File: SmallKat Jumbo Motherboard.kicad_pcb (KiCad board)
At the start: 4 copper layers, 80 x 80 mm, 49 parts, among them IC1 TPS562201DDCR, IC2 TPS562201DDCR, J1 Conn_01x06_Male, J10 Conn_01x06_Male, J11 Conn_01x06_Male, J12 Conn_01x04_Male, J13 Conn_01x02_Male, J14 Conn_01x04_Male, J15 Conn_01x04_Male, J16 Conn_01x06_Male, J2 Conn_01x06_Male, J3 Conn_01x06_Male, J4 Conn_01x06_Male, J5 Conn_01x06_Male, J6 Conn_01x06_Male, J7 Conn_01x06_Male, J8 Conn_01x06_Male, J9 Conn_01x06_Male, U1 STM32H753IITx, Y1 32.768khz, Y2 32MHZ

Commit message: Added mounting holes
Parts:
- added REF**: MountingHole_3.2mm_M3, MountingHole:MountingHole_3.2mm_M3, F.Cu at (76.5, 3.50)
- added REF**: MountingHole_3.2mm_M3, MountingHole:MountingHole_3.2mm_M3, F.Cu at (3.50, 3.50)
- added REF**: MountingHole_3.2mm_M3, MountingHole:MountingHole_3.2mm_M3, F.Cu at (76.5, 76.5)
- added REF**: MountingHole_3.2mm_M3, MountingHole:MountingHole_3.2mm_M3, F.Cu at (3.50, 76.5)
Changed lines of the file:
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@@
     (tracks 1078)
     (zones 0)
-    (modules 49)
+    (modules 53)
     (nets 56)
   )
@@
     (add_net USBDP)
   )
+  (module MountingHole:MountingHole_3.2mm_M3 (layer F.Cu)
+    (at 76.5 3.5)
+    (descr "Mounting Hole 3.2mm, no annular, M3")
+    (tags "mounting hole 3.2mm no annular m3")
+    (attr virtual)
+    (fp_text reference REF** (at 0 -4.2) (layer F.SilkS)
+      (effects (font (size 1 1) (thickness 0.15)))
+    )
+    (fp_text value MountingHole_3.2mm_M3 (at 0 4.2) (layer F.Fab)
+      (effects (font (size 1 1) (thickness 0.15)))
+    )
+    (fp_circle (center 0 0) (end 3.45 0) (layer F.CrtYd) (width 0.05))
+    (fp_circle (center 0 0) (end 3.2 0) (layer Cmts.User) (width 0.15))
+    (fp_text user %R (at 0.3 0) (layer F.Fab)
+      (effects (font (size 1 1) (thickness 0.15)))
+    )
+    (pad 1 np_thru_hole circle (at 0 0) (size 3.2 3.2) (drill 3.2) (layers *.Cu *.Mask))
+  )
   (module Crystal:Crystal_SMD_2012-2Pin_2.0x1.2mm (layer F.Cu)
     (at 24.79 33.81 270)
@@
     )
   )
+  (module MountingHole:MountingHole_3.2mm_M3 (layer F.Cu)
+    (at 3.5 3.5)
+    (descr "Mounting Hole 3.2mm, no annular, M3")
+    (tags "mounting hole 3.2mm no annular m3")
+    (attr virtual)
+    (fp_text reference REF** (at 0 -4.2) (layer F.SilkS)
+      (effects (font (size 1 1) (thickness 0.15)))
+    )
+    (fp_text value MountingHole_3.2mm_M3 (at 0 4.2) (layer F.Fab)
+      (effects (font (size 1 1) (thickness 0.15)))
+    )
+    (fp_text user %R (at 0.3 0) (layer F.Fab)
+      (effects (font (size 1 1) (thickness 0.15)))
+    )
+    (fp_circle (center 0 0) (end 3.2 0) (layer Cmts.User) (width 0.15))
+    (fp_circle (center 0 0) (end 3.45 0) (layer F.CrtYd) (width 0.05))
+    (pad 1 np_thru_hole circle (at 0 0) (size 3.2 3.2) (drill 3.2) (layers *.Cu *.Mask))
+  )
+  (module MountingHole:MountingHole_3.2mm_M3 (layer F.Cu)
+    (at 76.5 76.5)
+    (descr "Mounting Hole 3.2mm, no annular, M3")
+    (tags "mounting hole 3.2mm no annular m3")
+    (attr virtual)
+    (fp_text reference REF** (at 0 -4.2) (layer F.SilkS)
+      (effects (font (size 1 1) (thickness 0.15)))
+    )
+    (fp_text value MountingHole_3.2mm_M3 (at 0 4.2) (layer F.Fab)
+      (effects (font (size 1 1) (thickness 0.15)))
+    )
+    (fp_circle (center 0 0) (end 3.45 0) (layer F.CrtYd) (width 0.05))
+    (fp_circle (center 0 0) (end 3.2 0) (layer Cmts.User) (width 0.15))
+    (fp_text user %R (at 0.3 0) (layer F.Fab)
+      (effects (font (size 1 1) (thickness 0.15)))
+    )
+    (pad 1 np_thru_hole circle (at 0 0) (size 3.2 3.2) (drill 3.2) (layers *.Cu *.Mask))
+  )
+  (module MountingHole:MountingHole_3.2mm_M3 (layer F.Cu)
+    (at 3.5 76.5)
+    (descr "Mounting Hole 3.2mm, no annular, M3")
+    (tags "mounting hole 3.2mm no annular m3")
+    (attr virtual)
+    (fp_text reference REF** (at 0 -4.2) (layer F.SilkS)
+      (effects (font (size 1 1) (thickness 0.15)))
+    )
+    (fp_text value MountingHole_3.2mm_M3 (at 0 4.2) (layer F.Fab)
+      (effects (font (size 1 1) (thickness 0.15)))
+    )
+    (fp_circle (center 0 0) (end 3.45 0) (layer F.CrtYd) (width 0.05))
+    (fp_circle (center 0 0) (end 3.2 0) (layer Cmts.User) (width 0.15))
+    (fp_text user %R (at 0.3 0) (layer F.Fab)
+      (effects (font (size 1 1) (thickness 0.15)))
+    )
+    (pad 1 np_thru_hole circle (at 0 0) (size 3.2 3.2) (drill 3.2) (layers *.Cu *.Mask))
+  )
   (gr_line (start 80 80) (end 80 0) (layer Edge.Cuts) (width 0.2))

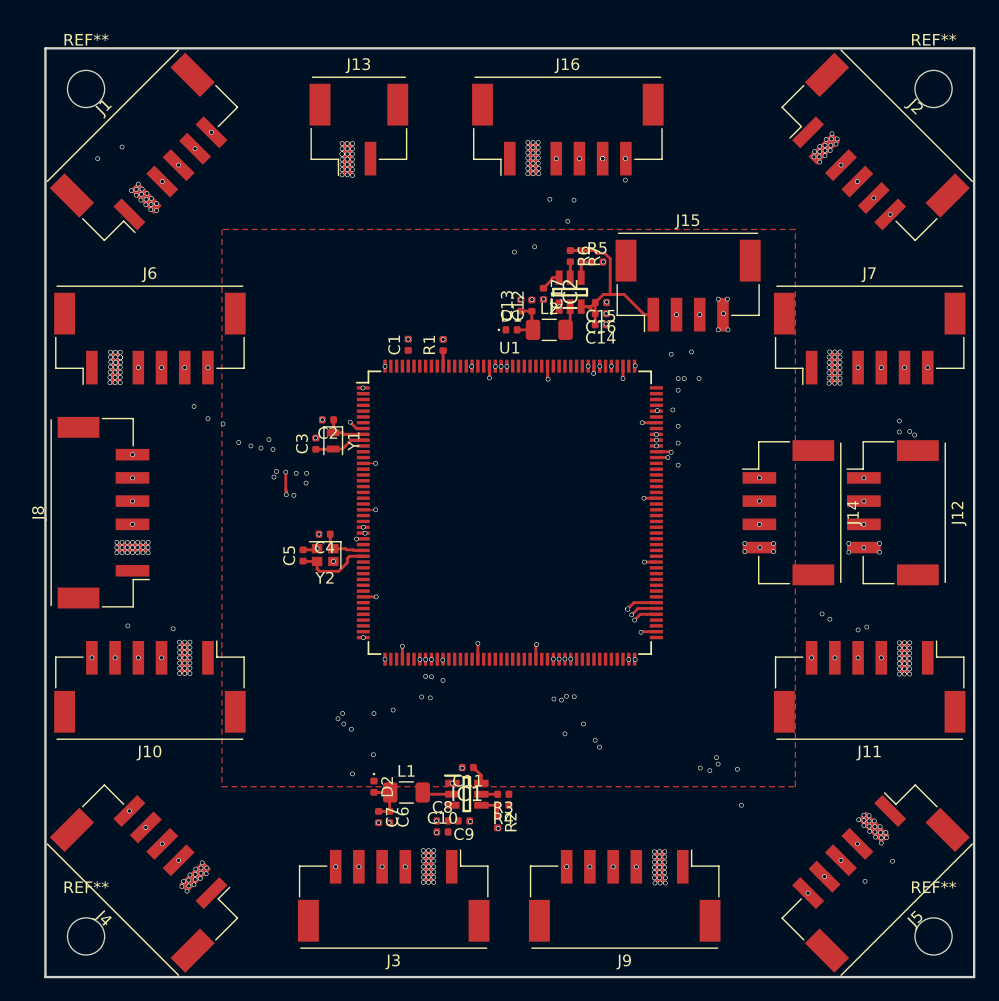
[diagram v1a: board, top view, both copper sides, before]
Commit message: fixed pinout
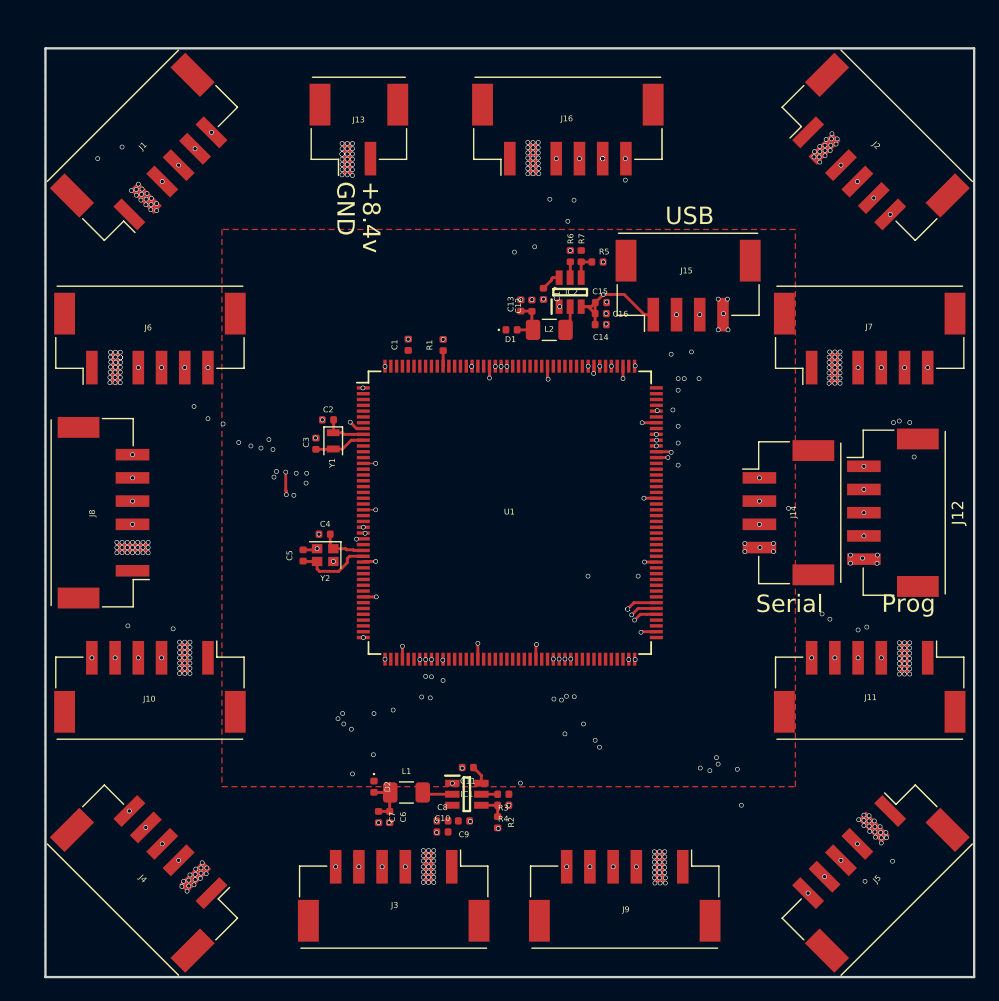
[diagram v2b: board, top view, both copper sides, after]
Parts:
- removed REF** (x4): MountingHole_3.2mm_M3, MountingHole:MountingHole_3.2mm_M3
- J12: value Conn_01x04_Male -> Conn_01x05_Male; footprint Connector_Molex:Molex_CLIK-Mate_502443-0470_1x04-1MP_P2.00mm_Vertical -> Connector_Molex:Molex_CLIK-Mate_502443-0570_1x05-1MP_P2.00mm_Vertical
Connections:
- J12 pad 1: SWCLK -> NRST
- J12 pad 2: SWDIO -> SWCLK
- J12 pad 3: +3V3 -> SWDIO
- J12 pad 4: GND -> +3V3
- R4 pad 1: +BATT -> +3V3
- R7 pad 1: +5V -> +3V3
- U1 pad 31: (no net) -> NRST
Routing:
- net NRST: track 0.00 -> 47.9 mm, vias 0 -> 5
- net +3V3: track 9.00 -> 11.7 mm, vias 2 -> 4
- net +5V: track 17.5 -> 15.7 mm, vias 0 -> 2
- net SCK5: track 123.7 -> 122.8 mm
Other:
- board text added: "+8.4v"
- board text added: "GND"
- board text added: "Keion Bisland Xavier Little Alex Tacescu"
- board text added: "Prog"
- board text added: "Serial"
- board text added: "SmallKat MQP Motherboard Rev. 1"
- board text added: "USB"

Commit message: Rev 2
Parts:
- removed C10, C11: 0.1UF, Capacitor_SMD:C_0402_1005Metric
- removed C15, C8, C9: 10UF, Capacitor_SMD:C_0402_1005Metric
- removed C6, C7: 22UF, Capacitor_SMD:C_0402_1005Metric
- removed IC1: TPS562201DDCR, TPS562201DDCR:SOT95P280X110-6N
- removed J11: Conn_01x06_Male, Connector_Molex:Molex_CLIK-Mate_502443-0670_1x06-1MP_P2.00mm_Vertical
- removed J12: Conn_01x05_Male, Connector_Molex:Molex_CLIK-Mate_502443-0570_1x05-1MP_P2.00mm_Vertical
- removed J13: Conn_01x02_Male, Connector_Molex:Molex_CLIK-Mate_502443-0270_1x02-1MP_P2.00mm_Vertical
- removed L1: 4.7UH, Inductor_SMD:L_1206_3216Metric
- added C18: 0.1uF, Capacitor_SMD:C_0402_1005Metric, F.Cu at (34.1, 43.3)
- added C19: 0.1uF, Capacitor_SMD:C_0402_1005Metric, F.Cu at (26.5, 29.8)
- added C20: 0.1uF, Capacitor_SMD:C_0402_1005Metric, F.Cu at (48.6, 35.4)
- added C21: 0.1uF, Capacitor_SMD:C_0402_1005Metric, F.Cu at (40.1, 21.3)
- added C22: 0.1uF, Capacitor_SMD:C_0402_1005Metric, F.Cu at (26.7, 35.9)
- added D3: LED, LED_SMD:LED_0603_1608Metric, F.Cu at (42.1, 16.9)
- added FB1: Ferrite_Bead, Inductor_SMD:L_0805_2012Metric, B.Cu at (24.2, 32.4)
- added H1: MountingHole, MountingHole:MountingHole_3.2mm_M3, F.Cu at (72.3, 61.0)
- added H2: MountingHole, MountingHole:MountingHole_3.2mm_M3, F.Cu at (71.1, 3.35)
- added H3: MountingHole, MountingHole:MountingHole_3.2mm_M3, F.Cu at (5.35, 13.3)
- added R10: 10k, Resistor_SMD:R_0402_1005Metric, F.Cu at (28.5, 27.0)
- added R11: 33R, Resistor_SMD:R_0402_1005Metric, F.Cu at (61.8, 54.0)
- added R12: 33R, Resistor_SMD:R_0402_1005Metric, F.Cu at (63.8, 54.1)
- added R8: 33R, Resistor_SMD:R_0402_1005Metric, F.Cu at (60.9, 10.2)
- added R9: 33R, Resistor_SMD:R_0402_1005Metric, F.Cu at (58.9, 10.2)
- C1: value 1UF -> 0.1uF
- C12, C13, C14, C16: footprint Capacitor_SMD:C_0402_1005Metric -> Capacitor_SMD:C_0805_2012Metric
- D1, D2: value 641-1675-1-ND -> LED; footprint Diode_SMD:D_0402_1005Metric -> LED_SMD:LED_0603_1608Metric
- J10, J9: value Conn_01x06_Male -> Conn_01x04_Male; footprint Connector_Molex:Molex_CLIK-Mate_502443-0670_1x06-1MP_P2.00mm_Vertical -> Connector_Molex:Molex_CLIK-Mate_502443-0470_1x04-1MP_P2.00mm_Vertical
- J8: value Conn_01x06_Male -> PRT-10474; footprint Connector_Molex:Molex_CLIK-Mate_502443-0670_1x06-1MP_P2.00mm_Vertical -> PRT-10474:SHDR2W320P716_1X2_1574X813X1588P
- L2: footprint Inductor_SMD:L_1206_3216Metric -> Inductor_SMD:L_0805_2012Metric_Pad1.15x1.40mm_HandSolder
- R1, R5: value 10K -> 10k
- R2, R3: value 10K -> 330R
- R4: value 33.2K -> 330R
- R7: value 33.2K -> 33.2k
- U1: value STM32H753IITx -> STM32H743VITx; footprint Package_QFP:LQFP-176_24x24mm_P0.5mm -> Package_QFP:LQFP-100_14x14mm_P0.5mm
- moved J5 71.0 mm to (5.00, 44.7), turned to 90 degrees
- moved J3 68.3 mm to (26.4, 4.80), turned to 0 degrees
- moved J1 62.8 mm to (46.2, 59.6), turned to 180 degrees
- moved J2 62.5 mm to (8.60, 4.80), turned to 0 degrees
- moved J10 54.0 mm to (62.8, 59.6)
- moved J9 49.5 mm to (70.1, 27.8), turned to 270 degrees
- moved D2 49.2 mm to (43.8, 16.9)
- moved R2 47.5 mm to (45.1, 19.5), turned to 90 degrees
- moved R4 45.8 mm to (42.1, 19.5), turned to 90 degrees
- moved R3 44.9 mm to (43.8, 19.6), turned to 90 degrees
- moved J6 39.2 mm to (27.4, 59.6), turned to 180 degrees
- moved J14 27.8 mm to (70.1, 12.9)
- moved C1 20.5 mm to (40.3, 44.0), turned to 225 degrees
- moved J7 19.9 mm to (70.2, 44.9), turned to 270 degrees
- moved J15 16.3 mm to (59.9, 4.80)
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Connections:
- C1 pad 2: GND -> MCU_GND
- C12 pad 1: Net-(C12-Pad1) -> +3V3
- C13 pad 1: Net-(C12-Pad1) -> +3V3
- C17 pad 2: GND -> Net-(C17-Pad2)
- C2 pad 2: GND -> MCU_GND
- C3 pad 2: GND -> MCU_GND
- C4 pad 2: GND -> MCU_GND
- C5 pad 2: GND -> MCU_GND
- D1 pad 1: +3V3 -> GND
- D1 pad 2: Net-(C12-Pad1) -> Net-(D1-Pad2)
- D2 pad 1: +3V3 -> GND
- D2 pad 2: Net-(C6-Pad1) -> Net-(D2-Pad2)
- IC2 pad 2: Net-(IC2-Pad2) -> Net-(C17-Pad2)
- J1 pad 3: SCK1 -> MISO1
- J1 pad 4: MISO1 -> MOSI1
- J1 pad 5: MOSI1 -> SCK1
- J1 pad 6: CS1_1 -> CS1
- J10 pad 1: +BATT -> +5V
- J10 pad 2: GND -> Net-(J10-Pad2)
- J10 pad 3: SCK5 -> Net-(J10-Pad3)
- J10 pad 4: MISO5 -> GND
- J15 pad 2: USBDM -> Net-(J15-Pad2)
- J15 pad 3: USBDP -> Net-(J15-Pad3)
- J16 pad 6: CS6 -> CS6_HEAD
- J2 pad 3: SCK1 -> MISO3
- J2 pad 4: MISO1 -> MOSI3
- J2 pad 5: MOSI1 -> SCK3
- J2 pad 6: CS1_2 -> CS3
- J3 pad 3: SCK2 -> SCK6
- J3 pad 4: MISO2 -> MISO6
- J3 pad 5: MOSI2 -> MOSI6
- J3 pad 6: CS2 -> CS6_TAIL
- J4 pad 3: SCK1 -> MISO2
- J4 pad 4: MISO1 -> MOSI2
- J4 pad 5: MOSI1 -> SCK2
- J4 pad 6: CS1_3 -> CS2
- J5 pad 3: SCK1 -> MISO4
- J5 pad 4: MISO1 -> MOSI4
- J5 pad 5: MOSI1 -> SCK4
- J5 pad 6: CS1_4 -> CS4
- J6 pad 3: SCK5 -> MISO1
- J6 pad 4: MISO5 -> MOSI1
- J6 pad 5: MOSI5 -> SCK1
- J6 pad 6: CS5_1 -> IMU1_CS
- J7 pad 3: SCK5 -> MISO2
- J7 pad 4: MISO5 -> MOSI2
- J7 pad 5: MOSI5 -> SCK2
- J7 pad 6: CS5_2 -> IMU2_CS
- J8 pad 1: +BATT -> GND
- J8 pad 2: GND -> +BATT
- J9 pad 1: +BATT -> SWCLK
- J9 pad 2: GND -> SWDIO
- J9 pad 3: SCK4 -> +3V3
- J9 pad 4: MISO4 -> GND
- L2 pad 1: Net-(C12-Pad1) -> +3V3
- L2 pad 2: Net-(IC2-Pad2) -> Net-(C17-Pad2)
- R2 pad 1: Net-(IC1-Pad4) -> LED1
- R2 pad 2: GND -> Net-(D1-Pad2)
- R3 pad 1: +BATT -> LED2
- R3 pad 2: Net-(IC1-Pad5) -> Net-(D2-Pad2)
- R4 pad 1: +3V3 -> LED3
- R4 pad 2: Net-(IC1-Pad4) -> Net-(D3-Pad2)
- U1 pad 1: CS5_1 -> SCK4
- U1 pad 10: OSCOUT_32 -> MCU_GND
- U1 pad 100: (no net) -> +3V3
- U1 pad 11: (no net) -> +3V3
- U1 pad 12: (no net) -> OSCIN
- U1 pad 13: (no net) -> OSCOUT
- U1 pad 14: GND -> Net-(U1-Pad14)
- U1 pad 15: +3V3 -> Net-(U1-Pad15)
- U1 pad 16: (no net) -> MOSI2
- U1 pad 17: (no net) -> MISO2
- U1 pad 18: (no net) -> CS2
- U1 pad 19: (no net) -> MCU_GND
- U1 pad 2: (no net) -> Net-(U1-Pad2)
- U1 pad 20: (no net) -> Net-(U1-Pad20)
- U1 pad 21: (no net) -> +3V3
- U1 pad 22: GND -> Net-(U1-Pad22)
- U1 pad 23: +3V3 -> IMU1_CS
- U1 pad 24: (no net) -> Net-(U1-Pad24)
- U1 pad 25: SCK5 -> Net-(U1-Pad25)
- U1 pad 26: MISO5 -> MCU_GND
- U1 pad 27: MOSI5 -> +3V3
- U1 pad 28: (no net) -> CS1
- U1 pad 29: OSCIN -> SCK1
- U1 pad 3: (no net) -> CS4
- U1 pad 30: OSCOUT -> MISO1
- U1 pad 31: NRST -> MOSI1
- U1 pad 32: (no net) -> Net-(U1-Pad32)
- U1 pad 33: (no net) -> Net-(U1-Pad33)
- U1 pad 34: (no net) -> Net-(U1-Pad34)
- U1 pad 35: (no net) -> Net-(U1-Pad35)
- U1 pad 36: +3V3 -> Net-(U1-Pad36)
- U1 pad 37: GND -> IMU2_CS
- U1 pad 38: (no net) -> Net-(U1-Pad38)
- U1 pad 39: +3V3 -> Net-(U1-Pad39)
- U1 pad 4: (no net) -> MISO4
- U1 pad 40: (no net) -> Net-(U1-Pad40)
- U1 pad 41: (no net) -> Net-(U1-Pad41)
- U1 pad 42: (no net) -> Net-(U1-Pad42)
- U1 pad 43: (no net) -> Net-(U1-Pad43)
- U1 pad 44: CS5_3 -> Net-(U1-Pad44)
- U1 pad 45: CS1_3 -> Net-(U1-Pad45)
- U1 pad 46: (no net) -> SCK2
- U1 pad 47: (no net) -> Net-(U1-Pad47)
- U1 pad 48: GND -> Net-(U1-Pad48)
- U1 pad 49: +3V3 -> MCU_GND
- U1 pad 5: (no net) -> MOSI4
- U1 pad 50: (no net) -> +3V3
- U1 pad 51: SCK1 -> Net-(U1-Pad51)
- U1 pad 52: MISO1 -> Net-(U1-Pad52)
- U1 pad 53: MOSI1 -> USB_HS_N
- U1 pad 54: (no net) -> USB_HS_P
- U1 pad 55: CS2 -> Net-(U1-Pad55)
- U1 pad 56: (no net) -> Net-(U1-Pad56)
- U1 pad 57: (no net) -> Net-(U1-Pad57)
- U1 pad 58: (no net) -> Net-(U1-Pad58)
- U1 pad 59: (no net) -> LED1
- U1 pad 6: (no net) -> +3V3
- U1 pad 60: (no net) -> LED2
- U1 pad 61: GND -> LED3
- U1 pad 62: +3V3 -> Net-(U1-Pad62)
- U1 pad 63: (no net) -> Net-(U1-Pad63)
- U1 pad 64: (no net) -> Net-(U1-Pad64)
- U1 pad 65: (no net) -> Net-(U1-Pad65)
- U1 pad 66: (no net) -> Net-(U1-Pad66)
- U1 pad 67: (no net) -> Net-(U1-Pad67)
- U1 pad 68: (no net) -> TX
- U1 pad 69: (no net) -> RX
- U1 pad 7: (no net) -> Net-(U1-Pad7)
- U1 pad 70: (no net) -> USB_FS_N
- U1 pad 71: GND -> USB_FS_P
- U1 pad 72: +3V3 -> SWDIO
- U1 pad 73: (no net) -> Net-(U1-Pad73)
- U1 pad 74: CS4 -> MCU_GND
- U1 pad 75: SCK4 -> +3V3
- U1 pad 76: MISO4 -> SWCLK
- U1 pad 77: MOSI4 -> CS3
- U1 pad 78: (no net) -> SCK3
- U1 pad 79: (no net) -> MISO3
- U1 pad 8: CS3 -> OSCIN_32
- U1 pad 80: (no net) -> MOSI3
- U1 pad 81: (no net) -> CS6_TAIL
- U1 pad 82: +3V3 -> Net-(U1-Pad82)
- U1 pad 83: (no net) -> Net-(U1-Pad83)
- U1 pad 84: (no net) -> Net-(U1-Pad84)
- U1 pad 85: (no net) -> Net-(U1-Pad85)
- U1 pad 86: (no net) -> Net-(U1-Pad86)
- U1 pad 87: CS1_4 -> Net-(U1-Pad87)
- U1 pad 88: CS5_4 -> CS6_HEAD
- U1 pad 89: (no net) -> SCK6
- U1 pad 9: OSCIN_32 -> OSCOUT_32
- U1 pad 90: GND -> MISO6
- U1 pad 91: +3V3 -> MOSI6
- U1 pad 92: (no net) -> CS6
- U1 pad 93: SCK2 -> Net-(U1-Pad93)
- U1 pad 94: MISO2 -> Net-(R1-Pad1)
- U1 pad 95: MOSI2 -> Net-(U1-Pad95)
- U1 pad 96: (no net) -> Net-(U1-Pad96)
- U1 pad 97: (no net) -> Net-(U1-Pad97)
- U1 pad 98: (no net) -> Net-(U1-Pad98)
- U1 pad 99: (no net) -> MCU_GND
- Y2 pad 2: GND -> MCU_GND
- Y2 pad 4: GND -> MCU_GND
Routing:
- net SCK1: track 221.0 -> 41.7 mm, vias 11 -> 2
- net MISO1: track 218.4 -> 40.6 mm, vias 11 -> 2
- net MOSI1: track 215.5 -> 41.9 mm, vias 9 -> 4
- net SCK5: track 122.8 -> 0.00 mm, vias 13 -> 0
- net MISO5: track 119.8 -> 0.00 mm, vias 14 -> 0
- net MOSI5: track 116.8 -> 0.00 mm, vias 8 -> 0
- net +3V3: track 11.7 -> 87.1 mm, vias 4 -> 22
- net +5V: track 15.7 -> 85.3 mm, vias 2 -> 21
- net NRST: track 47.9 -> 0.00 mm, vias 5 -> 0
- net USB_FS_P: track 0.00 -> 43.9 mm, vias 0 -> 2
- net USB_FS_N: track 0.00 -> 42.6 mm, vias 0 -> 2
- net GND: track 16.3 -> 56.1 mm, vias 309 -> 65
- net SCK2: track 45.6 -> 78.1 mm, vias 2 -> 4
- net IMU2_CS: track 0.00 -> 30.2 mm, vias 0 -> 4
- net CS6_HEAD: track 0.00 -> 29.9 mm, vias 0 -> 2
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- added copper zone on In1.Cu, net +3V3
- added copper zone on In1.Cu, net +BATT
- added copper zone on In2.Cu, net GND
- added copper zone on B.Cu, net MCU_GND
- removed copper zone on In2.Cu, net +BATT
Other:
- board size 80 x 80 mm -> 75 x 65 mm
- board text added: "+8.4V"
- board text added: "Gnd"
- board text added: "Head"
- board text added: "IMU"
- board text added: "Keion Bisland"
- board text added: "LEG"
- board text added: "Programming"
- board text added: "SmallKat MQP Motherboard"
- board text added: "Tail"
- board text added: "USB FS"
- board text added: "USB HS"
- board text added: "rev2"
- board text removed: "+8.4v"
- board text removed: "GND"
- board text removed: "Keion Bisland Xavier Little Alex Tacescu"
- board text removed: "Prog"
- board text removed: "SmallKat MQP Motherboard Rev. 1"
- board text removed: "USB"

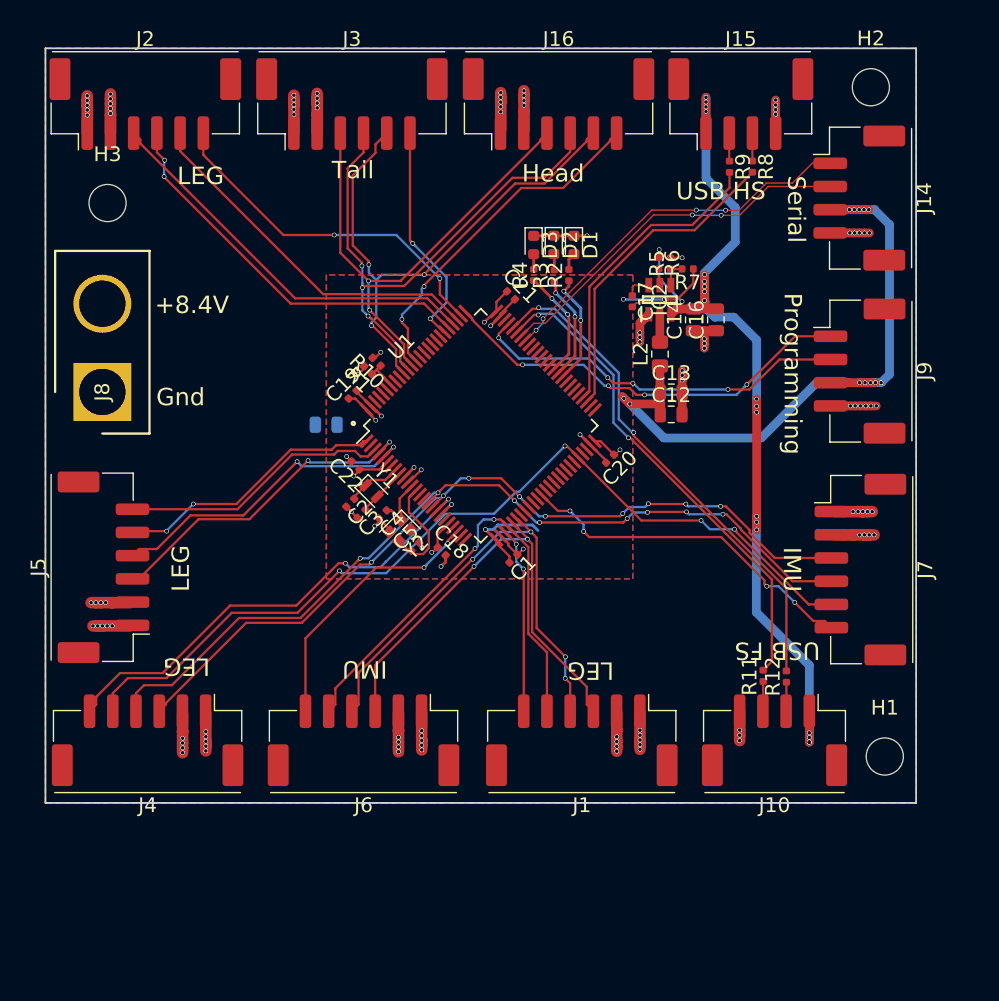
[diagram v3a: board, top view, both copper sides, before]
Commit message: Updated xt-60 plug footprint
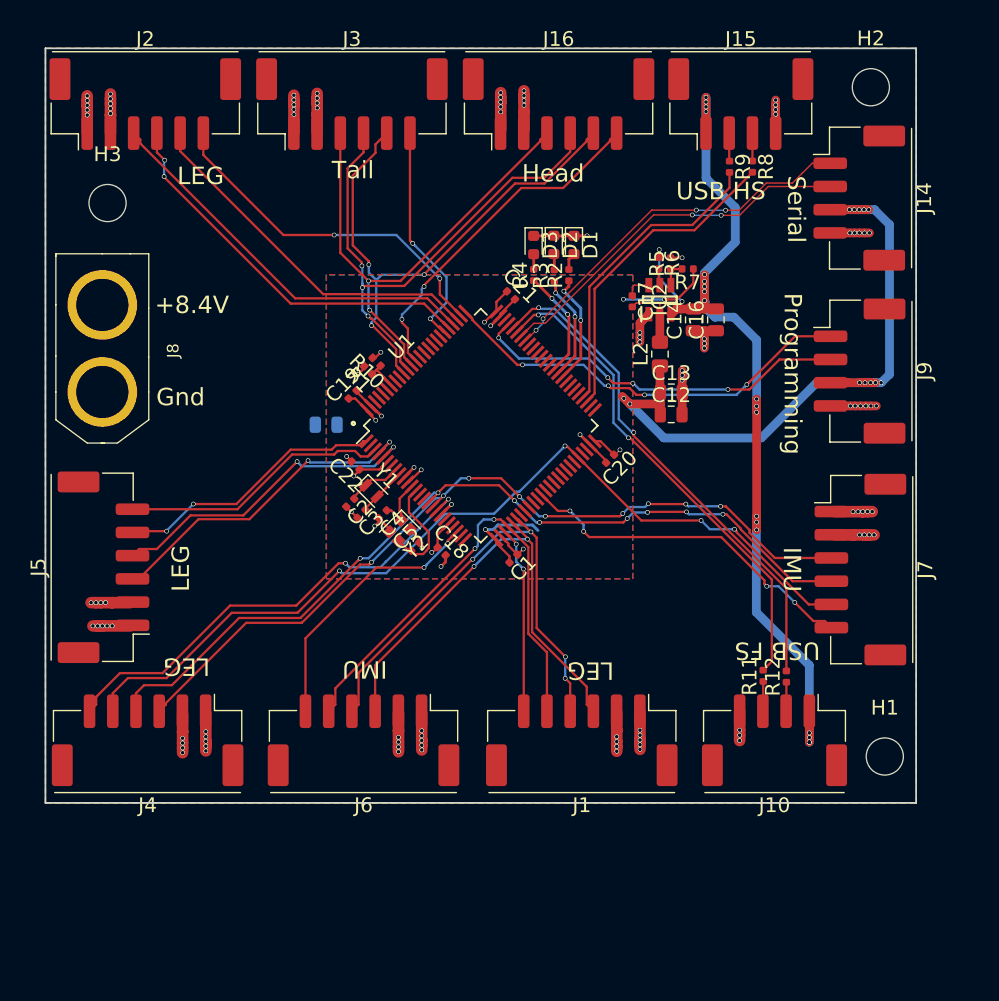
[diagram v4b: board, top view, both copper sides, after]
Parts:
- J8: footprint PRT-10474:SHDR2W320P716_1X2_1574X813X1588P -> xt-60:XT60
